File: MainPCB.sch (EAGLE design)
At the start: 80 parts, among them J2 DCJ0202, J3 FEMALE 2x3, X1 8MHz

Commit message: major changes
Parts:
- removed C11, C24, C25, C26: 0.1uF, SparkFun-Capacitors:0.1UF-0603-100V-10%
- removed JP1: (no value), pinhead:PINHD-2X6
- removed R17: 1k, SparkFun-Resistors:1KOHM-0603-1/10W-1%
- removed R18, R19: 100, SparkFun-Resistors:100KOHM-0603-1/10W-1%
- removed S2, S3: MOMENTARY-SWITCH-SPST-SMD-6.0X3.5MM, SparkFun-Switches:MOMENTARY-SWITCH-SPST-SMD-6.0X3.5MM
- removed U$7: ESP32, SeniorDesignParts:ESP32
- added J4: (no value), SparkFun-Connectors:CONN_04X2
- added JP5: (no value), pinhead:PINHD-1X8
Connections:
- removed net EN: C24.1, C26.1, R17.1, S2.2, U$7.EN
- removed net IO0: C25.1, S3.2, U$7.IO0
- removed net N$10: R19.2, U$7.RXD0
- removed net N$8: R18.2, U$7.TXD0
- new net IRQ: JP5.4
- new net RST: JP5.2
- new net SCK: JP5.7
- new net SDA: JP5.8
- net 3.3V: now also JP5.1; no longer C11.1, JP1.1, R17.2, U$7.3V3
- net GND: now also JP5.3; no longer C11.2, C24.2, C25.2, C26.2, JP1.11, S2.1, S3.1, U$7.GND1, U$7.GND2, U$7.GND3, U$7.P_GND
- net MISO: now also JP5.5; no longer JP1.5
- net MOSI: now also JP5.6; no longer JP1.2
- net RX_ESP: no longer R19.1
- net SCLK: no longer JP1.6
- net SS: no longer JP1.10
- net TX_ESP: no longer R18.1
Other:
- note added: "WiFi Dev Board Connections"

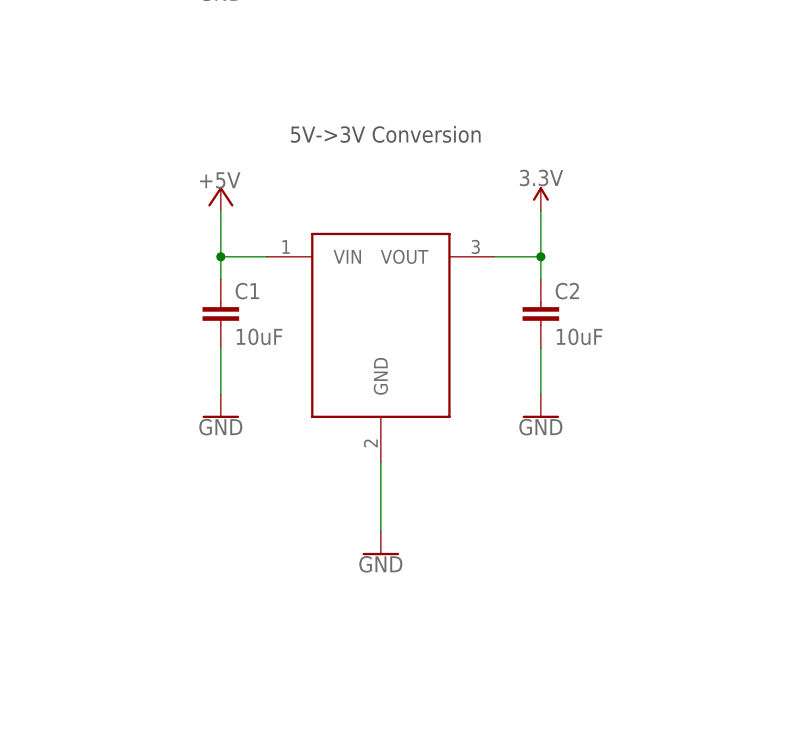
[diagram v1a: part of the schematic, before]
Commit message: 3.3V reguator
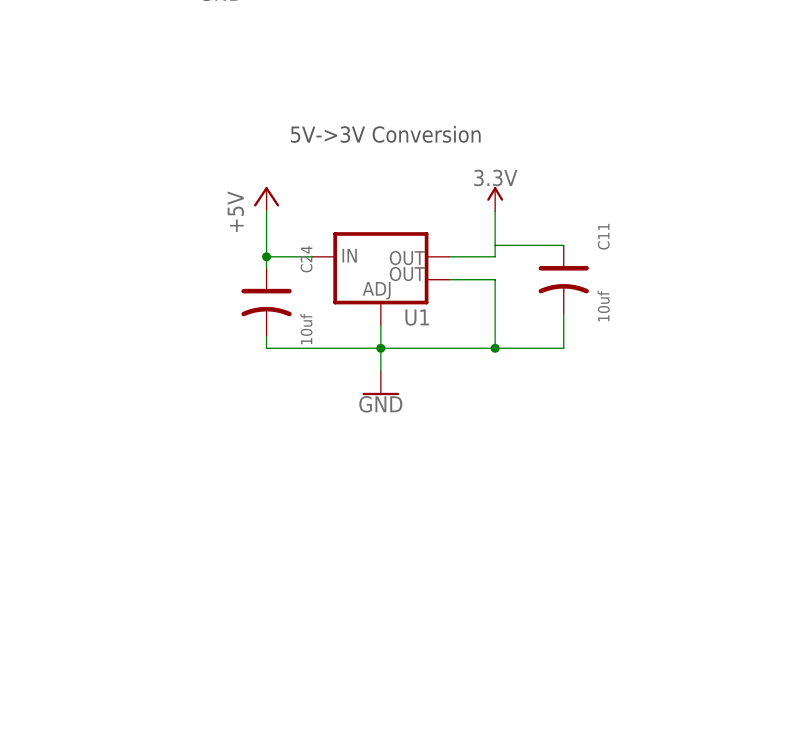
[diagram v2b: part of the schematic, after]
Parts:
- removed C1, C2: 10uF, SparkFun-Capacitors:10UF-0805-10V-10%
- removed U$4: AP7363, SeniorDesignParts:AP7363
- added C11, C24: 10uf, Seeed-Capacitor:TANTALUM-SMD-10UF-10V-10%(AVX-A)
- added U1: (no value), SparkFun-IC-Power:V_REG_LM1117SOT223
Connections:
- net +5V: now also C24.+, U1.IN; no longer C1.1, U$4.VIN
- net 3.3V: now also C11.+, U1.OUT; no longer C2.1, U$4.VOUT
- net GND: now also C11.-, C24.-, U1.ADJ, U1.OUT@1; no longer C1.2, C2.2, U$4.GND
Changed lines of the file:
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@@
 <part name="FRAME4" library="frames" library_urn="urn:adsk.eagle:library:229" deviceset="A4L-LOC" device=""/>
 <part name="U$3" library="SeniorDesignParts" deviceset="LM2576" device=""/>
-<part name="U$4" library="SeniorDesignParts" deviceset="AP7363" device=""/>
-<part name="GND3" library="SparkFun-PowerSymbols" library_urn="urn:adsk.eagle:library:530" deviceset="GND" device=""/>
-<part name="C1" library="SparkFun-Capacitors" library_urn="urn:adsk.eagle:library:510" deviceset="10UF" device="-0805-10V-10%" package3d_urn="urn:adsk.eagle:package:37429/1" value="10uF"/>
-<part name="C2" library="SparkFun-Capacitors" library_urn="urn:adsk.eagle:library:510" deviceset="10UF" device="-0805-10V-10%" package3d_urn="urn:adsk.eagle:package:37429/1" value="10uF"/>
-<part name="GND4" library="SparkFun-PowerSymbols" library_urn="urn:adsk.eagle:library:530" deviceset="GND" device=""/>
-<part name="GND5" library="SparkFun-PowerSymbols" library_urn="urn:adsk.eagle:library:530" deviceset="GND" device=""/>
-<part name="P+2" library="supply1" library_urn="urn:adsk.eagle:library:371" deviceset="+5V" device=""/>
-<part name="SUPPLY1" library="SparkFun-PowerSymbols" library_urn="urn:adsk.eagle:library:530" deviceset="3.3V" device=""/>
 <part name="SUPPLY2" library="SparkFun-PowerSymbols" library_urn="urn:adsk.eagle:library:530" deviceset="3.3V" device=""/>
 <part name="C3" library="SparkFun-Capacitors" library_urn="urn:adsk.eagle:library:510" deviceset="100UF-POLAR" device="-25V-20%(ELEC)" package3d_urn="urn:adsk.eagle:package:37420/1" value="100uF"/>
@@
 <part name="SUPPLY3" library="SparkFun-PowerSymbols" library_urn="urn:adsk.eagle:library:530" deviceset="3.3V" device=""/>
 <part name="GND9" library="supply1" library_urn="urn:adsk.eagle:library:371" deviceset="GND" device=""/>
+<part name="U1" library="SparkFun-IC-Power" library_urn="urn:adsk.eagle:library:526" deviceset="V_REG_LM1117" device="SOT223" package3d_urn="urn:adsk.eagle:package:39069/1"/>
+<part name="GND10" library="SparkFun-PowerSymbols" library_urn="urn:adsk.eagle:library:530" deviceset="GND" device=""/>
+<part name="P+5" library="supply1" library_urn="urn:adsk.eagle:library:371" deviceset="+5V" device=""/>
+<part name="SUPPLY4" library="SparkFun-PowerSymbols" library_urn="urn:adsk.eagle:library:530" deviceset="3.3V" device=""/>
+<part name="C11" library="Seeed-Capacitor" library_urn="urn:adsk.eagle:library:464" deviceset="TANTALUM-SMD-10UF-10V-10%(AVX-A)" device="" package3d_urn="urn:adsk.eagle:package:32380/1" value="10uf"/>
+<part name="C24" library="Seeed-Capacitor" library_urn="urn:adsk.eagle:library:464" deviceset="TANTALUM-SMD-10UF-10V-10%(AVX-A)" device="" package3d_urn="urn:adsk.eagle:package:32380/1" value="10uf"/>
 </parts>
 <sheets>
@@
 </instance>
 <instance part="U$3" gate="G$1" x="63.5" y="327.66"/>
-<instance part="U$4" gate="G$1" x="93.98" y="266.7"/>
-<instance part="GND3" gate="1" x="93.98" y="236.22">
-<attribute name="VALUE" x="93.98" y="235.966" size="1.778" layer="96" align="top-center"/>
-</instance>
-<instance part="C1" gate="G$1" x="76.2" y="261.62">
-<attribute name="NAME" x="77.724" y="264.541" size="1.778" layer="95" font="vector"/>
-<attribute name="VALUE" x="77.724" y="259.461" size="1.778" layer="96" font="vector"/>
-</instance>
-<instance part="C2" gate="G$1" x="111.76" y="261.62">
-<attribute name="NAME" x="113.284" y="264.541" size="1.778" layer="95" font="vector"/>
-<attribute name="VALUE" x="113.284" y="259.461" size="1.778" layer="96" font="vector"/>
-</instance>
-<instance part="GND4" gate="1" x="76.2" y="251.46">
-<attribute name="VALUE" x="76.2" y="251.206" size="1.778" layer="96" align="top-center"/>
-</instance>
-<instance part="GND5" gate="1" x="111.76" y="251.46">
-<attribute name="VALUE" x="111.76" y="251.206" size="1.778" layer="96" align="top-center"/>
-</instance>
-<instance part="P+2" gate="1" x="76.2" y="276.86">
-<attribute name="VALUE" x="73.66" y="276.86" size="1.778" layer="96"/>
-</instance>
-<instance part="SUPPLY1" gate="G$1" x="111.76" y="274.32">
-<attribute name="VALUE" x="111.76" y="277.114" size="1.778" layer="96" align="bottom-center"/>
-</instance>
 <instance part="SUPPLY2" gate="G$1" x="342.9" y="154.94">
 <attribute name="VALUE" x="342.9" y="157.734" size="1.778" layer="96" align="bottom-center"/>
@@
 <instance part="GND9" gate="1" x="388.62" y="53.34">
 <attribute name="VALUE" x="386.08" y="50.8" size="1.778" layer="96"/>
+</instance>
+<instance part="U1" gate="G$1" x="93.98" y="269.24">
+<attribute name="NAME" x="96.52" y="261.62" size="1.778" layer="95" font="vector"/>
+<attribute name="VALUE" x="96.52" y="259.08" size="1.778" layer="96" font="vector"/>
+</instance>
+<instance part="GND10" gate="1" x="93.98" y="254">
+<attribute name="VALUE" x="93.98" y="253.746" size="1.778" layer="96" align="top-center"/>
+</instance>
+<instance part="P+5" gate="1" x="81.28" y="276.86">
+<attribute name="VALUE" x="78.74" y="271.78" size="1.778" layer="96" rot="R90"/>
+</instance>
+<instance part="SUPPLY4" gate="G$1" x="106.68" y="274.32">
+<attribute name="VALUE" x="106.68" y="277.114" size="1.778" layer="96" align="bottom-center"/>
+</instance>
+<instance part="C11" gate="G$1" x="114.3" y="266.7" rot="R270">
+<attribute name="NAME" x="118.11" y="273.05" size="1.27" layer="95" ratio="10" rot="R270"/>
+<attribute name="VALUE" x="118.11" y="265.43" size="1.27" layer="96" ratio="10" rot="R270"/>
+</instance>
+<instance part="C24" gate="G$1" x="81.28" y="264.16" rot="R270">
+<attribute name="NAME" x="85.09" y="270.51" size="1.27" layer="95" ratio="10" rot="R270"/>
+<attribute name="VALUE" x="85.09" y="262.89" size="1.27" layer="96" ratio="10" rot="R270"/>
 </instance>
 </instances>
@@
 <pinref part="GND2" gate="1" pin="GND"/>
 <label x="312.42" y="152.4" size="1.778" layer="95"/>
-</segment>
-<segment>
-<pinref part="GND3" gate="1" pin="GND"/>
-<pinref part="U$4" gate="G$1" pin="GND"/>
-<wire x1="93.98" y1="246.38" x2="93.98" y2="238.76" width="0.1524" layer="91"/>
-</segment>
-<segment>
-<pinref part="C1" gate="G$1" pin="2"/>
-<pinref part="GND4" gate="1" pin="GND"/>
-<wire x1="76.2" y1="259.08" x2="76.2" y2="254" width="0.1524" layer="91"/>
-</segment>
-<segment>
-<pinref part="C2" gate="G$1" pin="2"/>
-<pinref part="GND5" gate="1" pin="GND"/>
-<wire x1="111.76" y1="259.08" x2="111.76" y2="254" width="0.1524" layer="91"/>
 </segment>
 <segment>
@@
 <wire x1="388.62" y1="58.42" x2="388.62" y2="55.88" width="0.1524" layer="91"/>
 </segment>
+<segment>
+<pinref part="U1" gate="G$1" pin="ADJ"/>
+<pinref part="GND10" gate="1" pin="GND"/>
+<wire x1="93.98" y1="261.62" x2="93.98" y2="259.08" width="0.1524" layer="91"/>
+<pinref part="C24" gate="G$1" pin="-"/>
+<wire x1="93.98" y1="259.08" x2="93.98" y2="256.54" width="0.1524" layer="91"/>
+<wire x1="81.28" y1="260.35" x2="81.28" y2="259.08" width="0.1524" layer="91"/>
+<wire x1="81.28" y1="259.08" x2="93.98" y2="259.08" width="0.1524" layer="91"/>
+<junction x="93.98" y="259.08"/>
+<pinref part="C11" gate="G$1" pin="-"/>
+<wire x1="114.3" y1="262.89" x2="114.3" y2="259.08" width="0.1524" layer="91"/>
+<wire x1="114.3" y1="259.08" x2="106.68" y2="259.08" width="0.1524" layer="91"/>
+<pinref part="U1" gate="G$1" pin="OUT@1"/>
+<wire x1="106.68" y1="259.08" x2="93.98" y2="259.08" width="0.1524" layer="91"/>
+<wire x1="101.6" y1="266.7" x2="106.68" y2="266.7" width="0.1524" layer="91"/>
+<wire x1="106.68" y1="266.7" x2="106.68" y2="259.08" width="0.1524" layer="91"/>
+<junction x="106.68" y="259.08"/>
+</segment>
 </net>
 <net name="+5V" class="0">
@@
 <pinref part="C9" gate="G$1" pin="1"/>
 <junction x="342.9" y="109.22"/>
-</segment>
-<segment>
-<pinref part="U$4" gate="G$1" pin="VIN"/>
-<pinref part="C1" gate="G$1" pin="1"/>
-<wire x1="81.28" y1="269.24" x2="76.2" y2="269.24" width="0.1524" layer="91"/>
-<wire x1="76.2" y1="269.24" x2="76.2" y2="266.7" width="0.1524" layer="91"/>
-<wire x1="76.2" y1="269.24" x2="76.2" y2="274.32" width="0.1524" layer="91"/>
-<junction x="76.2" y="269.24"/>
-<pinref part="P+2" gate="1" pin="+5V"/>
 </segment>
 <segment>
@@
 <pinref part="P+3" gate="1" pin="+5V"/>
 </segment>
+<segment>
+<pinref part="U1" gate="G$1" pin="IN"/>
+<wire x1="86.36" y1="269.24" x2="81.28" y2="269.24" width="0.1524" layer="91"/>
+<wire x1="81.28" y1="269.24" x2="81.28" y2="274.32" width="0.1524" layer="91"/>
+<pinref part="P+5" gate="1" pin="+5V"/>
+<pinref part="C24" gate="G$1" pin="+"/>
+<wire x1="81.28" y1="269.24" x2="81.28" y2="267.97" width="0.1524" layer="91"/>
+<junction x="81.28" y="269.24"/>
+</segment>
 </net>
 <net name="RS" class="0">
@@
 </net>
 <net name="3.3V" class="0">
-<segment>
-<pinref part="U$4" gate="G$1" pin="VOUT"/>
-<pinref part="C2" gate="G$1" pin="1"/>
-<wire x1="106.68" y1="269.24" x2="111.76" y2="269.24" width="0.1524" layer="91"/>
-<wire x1="111.76" y1="269.24" x2="111.76" y2="266.7" width="0.1524" layer="91"/>
-<wire x1="111.76" y1="269.24" x2="111.76" y2="274.32" width="0.1524" layer="91"/>
-<junction x="111.76" y="269.24"/>
-<pinref part="SUPPLY1" gate="G$1" pin="3.3V"/>
-</segment>
 <segment>
 <pinref part="J1" gate="G$1" pin="15"/>
@@
 <wire x1="401.32" y1="63.5" x2="401.32" y2="66.04" width="0.1524" layer="91"/>
 </segment>
+<segment>
+<pinref part="U1" gate="G$1" pin="OUT"/>
+<wire x1="101.6" y1="269.24" x2="106.68" y2="269.24" width="0.1524" layer="91"/>
+<wire x1="106.68" y1="269.24" x2="106.68" y2="270.51" width="0.1524" layer="91"/>
+<pinref part="SUPPLY4" gate="G$1" pin="3.3V"/>
+<pinref part="C11" gate="G$1" pin="+"/>
+<wire x1="106.68" y1="270.51" x2="106.68" y2="274.32" width="0.1524" layer="91"/>
+<wire x1="106.68" y1="270.51" x2="114.3" y2="270.51" width="0.1524" layer="91"/>
+</segment>
 </net>

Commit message: yay purty
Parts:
- removed H1, H5: STAND-OFF, SparkFun-Hardware:STAND-OFF
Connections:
- removed net SS: U$1.PC6
- new net EN: J4.3
- new net FB1: U$9.4IN-, U$9.4OUT
- new net FB2: U$2.4IN-, U$2.4OUT
- new net FB3: U$10.4IN-, U$10.4OUT
- new net RST_ESP: J4.5
- net 3.3V: now also J4.7
- net GND: now also J4.2, U$10.4IN+, U$2.4IN+, U$9.4IN+
- net RX_ESP: now also J4.8
- net SDA: now also U$1.PC6
- net TX_ESP: now also J4.1
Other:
- moved on the sheet: C18, C19, C20, R7, R8, R9, U$10
